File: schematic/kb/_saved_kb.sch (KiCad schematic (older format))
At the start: 3 parts, among them P1 USB_A, SW1 Switch_SPDT_x2

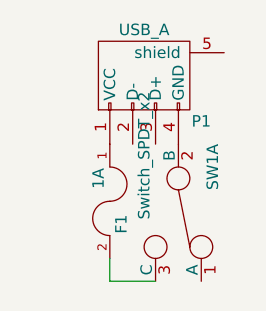
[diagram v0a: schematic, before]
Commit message: Added a red LED and matching resistor to warn user when USB splitter is missing
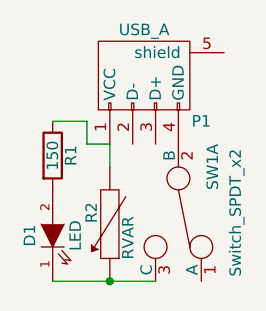
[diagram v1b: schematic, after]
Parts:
- removed F1: 1A, Resistors_SMD:R_1812, symbol FUSE
- added D1: LED, LEDs:LED-0603, symbol LED
- added R1: 150, Resistors_SMD:R_0805, symbol R
- added R2: RVAR, Resistors_SMD:R_1812, symbol RVAR
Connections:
- net at P1.1 (VCC): now also R1.1, R2.2
- net at SW1.3 (C): now also D1.1 (K), R2.1
- new net: D1.2 (A), R1.2
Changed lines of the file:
@@
 EESchema Schematic File Version 2
+LIBS:74xgxx
+LIBS:74xx
+LIBS:ac-dc
+LIBS:actel
+LIBS:adc-dac
+LIBS:Altera
+LIBS:analog_devices
+LIBS:analog_switches
+LIBS:atmel
+LIBS:audio
+LIBS:brooktre
+LIBS:cmos4000
+LIBS:cmos_ieee
+LIBS:conn
+LIBS:contrib
+LIBS:cypress
+LIBS:dc-dc
+LIBS:device
+LIBS:digital-audio
+LIBS:diode
+LIBS:display
+LIBS:dsp
+LIBS:elec-unifil
+LIBS:ESD_Protection
+LIBS:ftdi
+LIBS:gennum
+LIBS:graphic
+LIBS:hc11
+LIBS:intel
+LIBS:interface
+LIBS:ir
+LIBS:Lattice
+LIBS:linear
+LIBS:logo
+LIBS:maxim
+LIBS:memory
+LIBS:microchip
+LIBS:microchip_dspic33dsc
+LIBS:microchip_pic10mcu
+LIBS:microchip_pic12mcu
+LIBS:microchip_pic16mcu
+LIBS:microchip_pic18mcu
+LIBS:microchip_pic32mcu
+LIBS:microcontrollers
+LIBS:motor_drivers
+LIBS:motorola
+LIBS:msp430
+LIBS:nordicsemi
+LIBS:nxp_armmcu
+LIBS:onsemi
+LIBS:opto
+LIBS:Oscillators
+LIBS:philips
 LIBS:power
-LIBS:device
+LIBS:powerint
+LIBS:Power_Management
+LIBS:pspice
+LIBS:references
+LIBS:regul
+LIBS:relays
+LIBS:rfcom
+LIBS:sensors
+LIBS:silabs
+LIBS:siliconi
+LIBS:stm8
+LIBS:stm32
+LIBS:supertex
+LIBS:switches
+LIBS:texas
+LIBS:transf
 LIBS:transistors
-LIBS:conn
-LIBS:linear
-LIBS:regul
-LIBS:74xx
-LIBS:cmos4000
-LIBS:adc-dac
-LIBS:memory
+LIBS:ttl_ieee
+LIBS:valves
+LIBS:video
+LIBS:Xicor
 LIBS:xilinx
-LIBS:microcontrollers
-LIBS:dsp
-LIBS:microchip
-LIBS:analog_switches
-LIBS:motorola
-LIBS:texas
-LIBS:intel
-LIBS:audio
-LIBS:interface
-LIBS:digital-audio
-LIBS:philips
-LIBS:display
-LIBS:cypress
-LIBS:siliconi
-LIBS:opto
-LIBS:atmel
-LIBS:contrib
-LIBS:valves
-LIBS:diodesinc
-LIBS:antenova
-LIBS:melexis
+LIBS:Zilog
+LIBS:generic
 LIBS:kb-cache
 EELAYER 25 0
@@
 P 5300 5050
 F 0 "SW1" H 5100 5200 50  0000 C CNN
-F 1 "Switch_SPDT_x2" H 5050 4900 50  0000 C CNN
+F 1 "Switch_SPDT_x2" H 5300 5300 50  0000 C CNN
 F 2 "Buttons_Switches_ThroughHole:SW_Micro_SPST" H 5300 5050 50  0001 C CNN
 F 3 "" H 5300 5050 50  0000 C CNN
@@
 $EndComp
 $Comp
-L FUSE F1
-U 1 1 56887A87
-P 5000 5000
-F 0 "F1" H 5100 5050 50  0000 C CNN
-F 1 "1A" H 4900 4950 50  0000 C CNN
-F 2 "Resistors_SMD:R_1812" H 5000 5000 50  0001 C CNN
-F 3 "" H 5000 5000 50  0000 C CNN
-	1    5000 5000
-	0    1    1    0
+L RVAR R2
+U 1 1 568AFDD9
+P 5000 5100
+F 0 "R2" V 5080 5050 50  0000 C CNN
+F 1 "RVAR" V 4920 5160 50  0000 C CNN
+F 2 "Resistors_SMD:R_1812" H 5000 5100 50  0001 C CNN
+F 3 "" H 5000 5100 50  0000 C CNN
+	1    5000 5100
+	-1   0    0    1
+$EndComp
+$Comp
+L R R1
+U 1 1 568AFE80
+P 4750 4800
+F 0 "R1" V 4830 4800 50  0000 C CNN
+F 1 "150" V 4750 4800 50  0000 C CNN
+F 2 "Resistors_SMD:R_0805" V 4680 4800 50  0001 C CNN
+F 3 "" H 4750 4800 50  0000 C CNN
+	1    4750 4800
+	1    0    0    -1
+$EndComp
+$Comp
+L LED D1
+U 1 1 568AFEBD
+P 4750 5150
+F 0 "D1" H 4750 5250 50  0000 C CNN
+F 1 "LED" H 4750 5050 50  0000 C CNN
+F 2 "LEDs:LED-0603" H 4750 5150 50  0001 C CNN
+F 3 "http://optoelectronics.liteon.com/upload/download/DS-22-99-0151/S_110_LTST-C190KRKT.pdf" H 4750 5150 50  0001 C CNN
+	1    4750 5150
+	0    -1   -1   0
 $EndComp
 Wire Wire Line
-	5000 5250 5000 5350
+	5000 4750 4900 4750
 Wire Wire Line
-	5000 5350 5200 5350
+	4900 4750 4900 4650
+Wire Wire Line
+	4900 4650 4750 4650
+Wire Wire Line
+	5000 4750 5000 4850
+Wire Wire Line
+	4750 5350 5200 5350
+Connection ~ 5000 5350
 $EndSCHEMATC
